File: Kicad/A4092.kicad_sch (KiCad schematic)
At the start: 0 parts

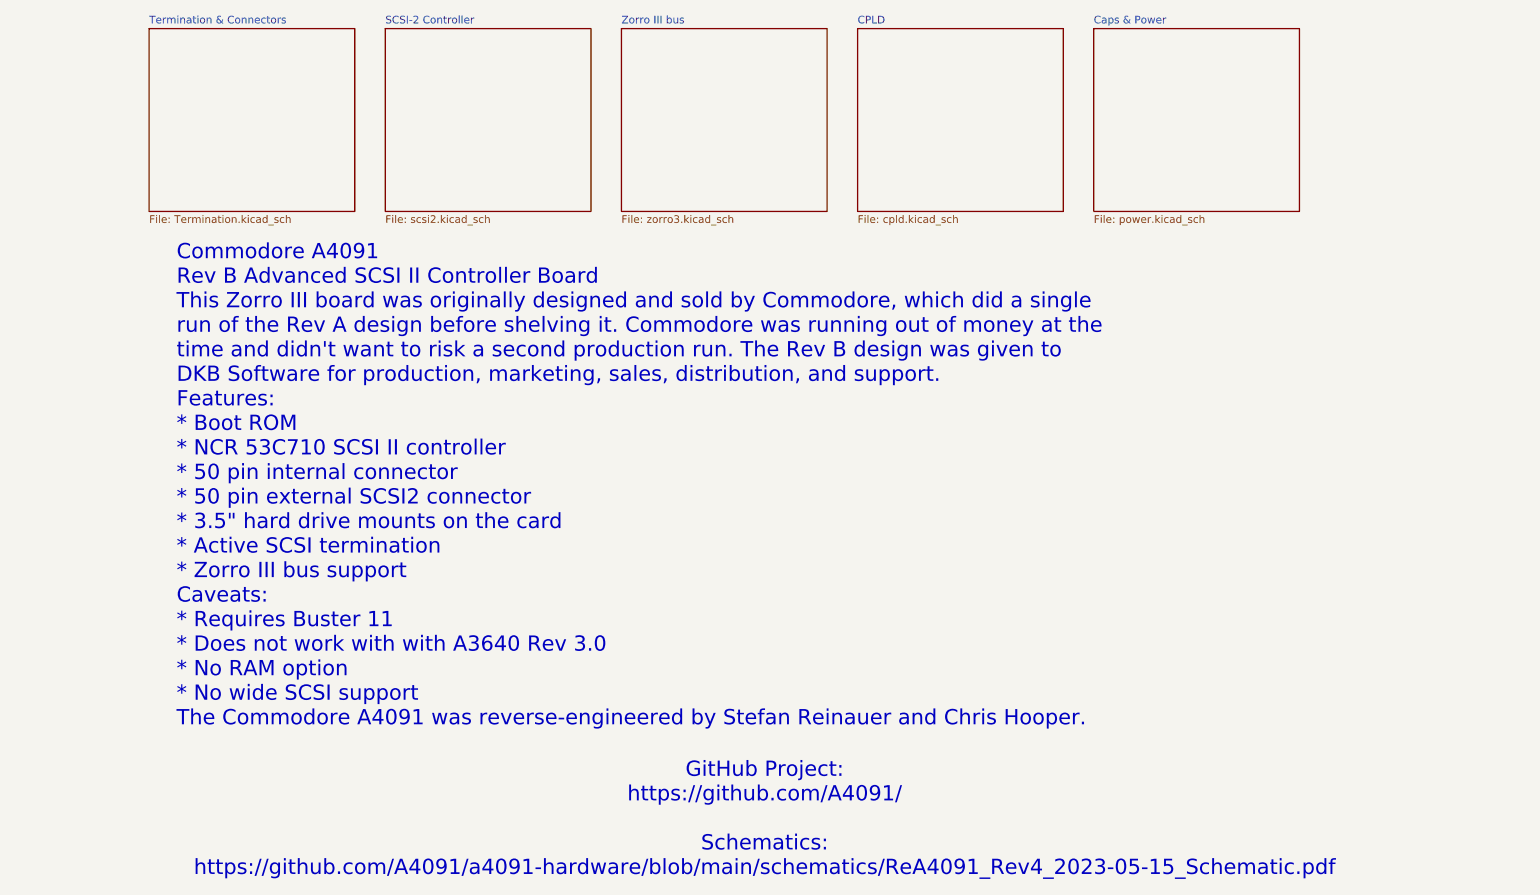
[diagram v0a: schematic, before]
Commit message: Update sheet, add pull down on ROM_CE
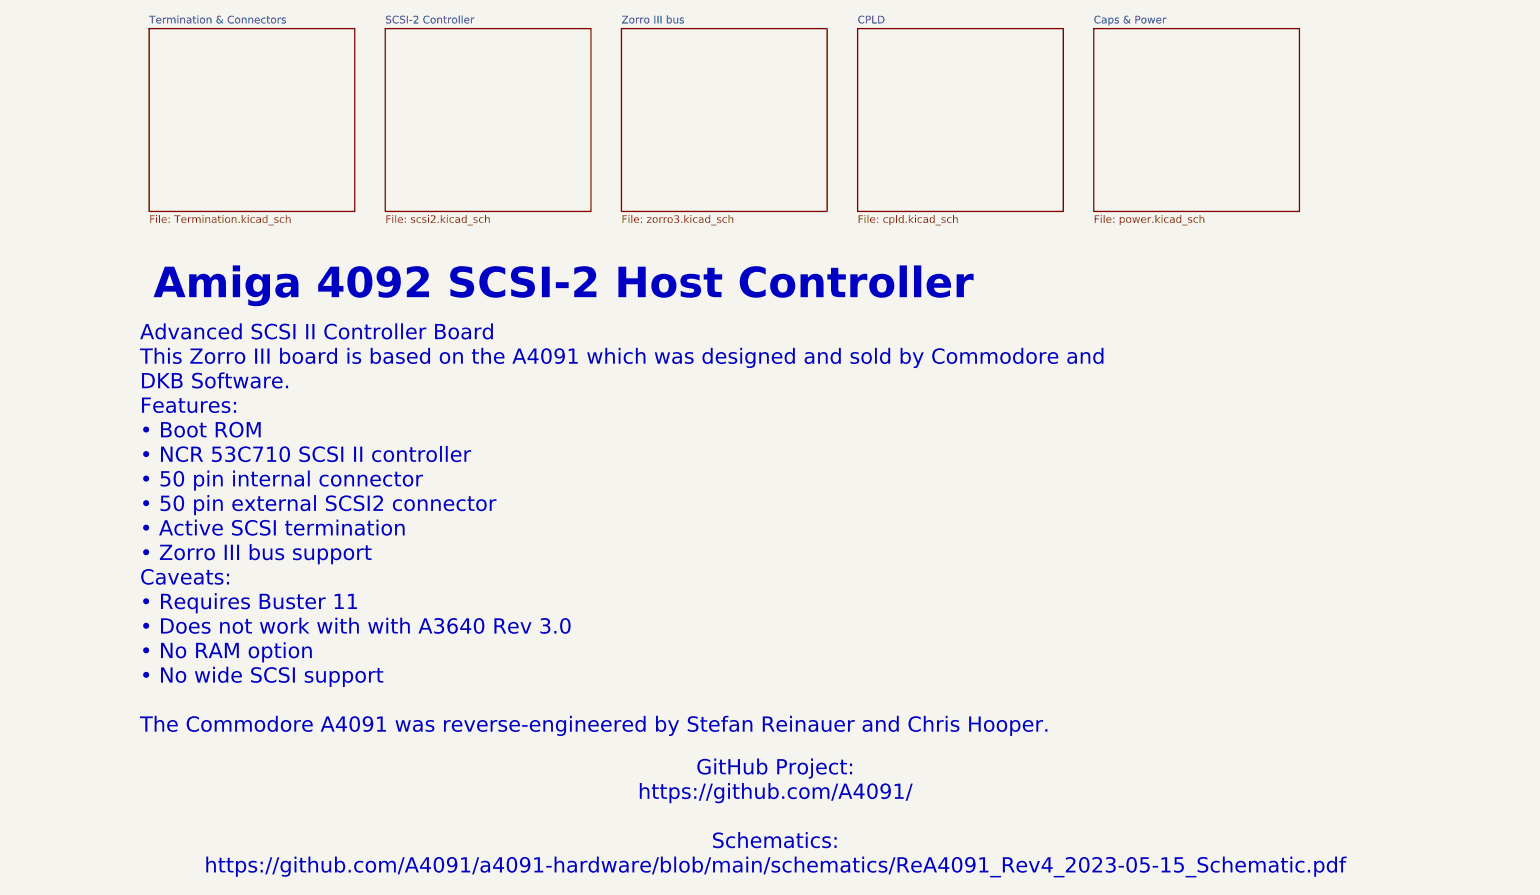
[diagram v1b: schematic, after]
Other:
- note added: "Advanced SCSI II Controller Board This Zorro III board is based on the A4091 which was designed and sold by Commodore and DKB Software. Features: • Boot ROM • NCR 53C710 SCSI II controller • 50 pin internal connector • 50 pin external SCSI2 connector • Active SCSI termination • Zorro III bus support Caveats: • Requires Buster 11 • Does not work with with A3640 Rev 3.0 • No RAM option • No wide SC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"
- note added: "Amiga 4092 SCSI-2 Host Controller"
- note removed: "Commodore A4091 Rev B Advanced SCSI II Controller Board This Zorro III board was originally designed and sold by Commodore, which did a single run of the Rev A design before shelving it. Commodore was running out of money at the time and didn't want to risk a second production run. The Rev B design was given to DKB Software for production, marketing, sales, distribution, and support. Features: * 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"
- company: (none) -> amiga.technology
- title: (none) -> A4092
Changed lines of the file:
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@@
 	(generator_version "9.0")
 	(paper "A4")
-	(text "Commodore A4091\nRev B Advanced SCSI II Controller Board\nThis Zorro III board was originally designed and sold by Commodore, which did a single\nrun of the Rev A design before shelving it. Commodore was running out of money at the\ntime and didn't want to risk a second production run. The Rev B design was given to\nDKB Software for production, marketing, sales, distribution, and support.\nFeatures:\n* Boot ROM\n* NCR 53C710 SCSI II controller\n* 50 pin internal connector\n* 50 pin external SCSI2 connector\n* 3.5\" hard drive mounts on the card\n* Active SCSI termination\n* Zorro III bus support\nCaveats:\n* Requires Buster 11\n* Does not work with with A3640 Rev 3.0\n* No RAM option\n* No wide SCSI support\nThe Commodore A4091 was reverse-engineered by Stefan Reinauer and Chris Hooper."
+	(title_block
+		(title "A4092")
+		(rev "PROTO0")
+		(company "amiga.technology")
+	)
+	(text "Advanced SCSI II Controller Board\nThis Zorro III board is based on the A4091 which was designed and sold by Commodore and\nDKB Software.\nFeatures:\n• Boot ROM\n• NCR 53C710 SCSI II controller\n• 50 pin internal connector\n• 50 pin external SCSI2 connector\n• Active SCSI termination\n• Zorro III bus support\nCaveats:\n• Requires Buster 11\n• Does not work with with A3640 Rev 3.0\n• No RAM option\n• No wide SCSI support\n\nThe Commodore A4091 was reverse-engineered by Stefan Reinauer and Chris Hooper. "
 		(exclude_from_sim no)
-		(at 57.912 97.79 0)
+		(at 51.816 105.156 0)
 		(effects
 			(font
@@
 	(text "GitHub Project:\nhttps://github.com/A4091/\n\nSchematics:\nhttps://github.com/A4091/a4091-hardware/blob/main/schematics/ReA4091_Rev4_2023-05-15_Schematic.pdf"
 		(exclude_from_sim no)
-		(at 155.956 153.416 0)
+		(at 157.734 153.162 0)
 		(effects
 			(font
@@
 			)
 		)
+	)
+	(text "Amiga 4092 SCSI-2 Host Controller\n"
+		(exclude_from_sim no)
+		(at 122.428 64.262 0)
+		(effects
+			(font
+				(size 5.08 5.08)
+				(thickness 1.016)
+				(bold yes)
+			)
+		)
